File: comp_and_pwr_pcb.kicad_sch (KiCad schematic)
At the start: 127 parts, among them IC1 TPS5430MDDAREP, IC2 ICM-42688-P, IC3 LTC4415EDHC#TRPBF, IC4 TPS259531DSGR, IC5 BMP388, IC6 W25Q32JVSSIQ, IC7 TPS62743YFPR, J1 USB4216-03-A, J2 BATTERY_CONN, J3 SWD_CONN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

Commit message: Replaced files and updated project
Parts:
- removed BWSMA-KE-P1, BWSMA-KE-P2: ~, Connector_Coaxial:SMA_BAT_Wireless_BWSMA-KWE-Z001, symbol My:BWSMA-KE-P001
- removed F3: 05200101Z, 05200101Z:05200101Z, symbol 05200101Z:05200101Z
- added F1: Fuse_Small, Fuse:Fuse_0402_1005Metric, symbol Device:Fuse_Small
- added J10, J9: Conn_01x02, TerminalBlock_4Ucon:TerminalBlock_4Ucon_1x02_P3.50mm_Vertical, symbol Connector_Generic:Conn_01x02
- added J11, J12: Conn_Coaxial, Connector_Coaxial:SMA_Molex_73251-2200_Horizontal, symbol Connector:Conn_Coaxial
- added R24: 4.7kΩ, Resistor_SMD:R_0402_1005Metric, symbol Device:R
- E22-400M22S1: footprint E22-400M22S1:E22-400MM22S -> E22-400M22S:E22-400M22S
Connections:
- net +3.3V: now also R24.1
- net +BATT: now also F1.2
- net GND: now also J10.2 (Pin_2), J11.2 (Ext), J12.2 (Ext), J9.2 (Pin_2); no longer Q7.2 (S), Q9.2 (S)
- net I2C_SCL: now also R24.2
- net at J2.2 (Pin_2): now also F1.1
- net at D5.2 (A2), U2.11 (RF_IN): now also J12.1 (In)
- net at E22-400M22S1.21 (ANT): now also J11.1 (In)
- new net: J9.1 (Pin_1), Q9.2 (S)
- new net: J10.1 (Pin_1), Q7.2 (S)
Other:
- moved on the sheet: D5, Q7, Q8, R57, R58, R59, R60, TX2

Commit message: Initial KiCad project commit
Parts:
- removed C14: 10uF, Capacitor_SMD:C_1206_3216Metric, symbol Device:C
- removed IC7: TPS62743YFPR, TPS62743YFPR:BGA8C40P2X4_87X156X53, symbol TPS62743YFPR:TPS62743YFPR
- added C20: 0.1uF, Capacitor_SMD:C_0402_1005Metric, symbol Device:C
- added C23: 4.7uF, Capacitor_SMD:C_0603_1608Metric, symbol Device:C
- added C24: 10uF, Capacitor_SMD:C_1206_3216Metric, symbol Device:C
- added H1, H2, H3, H4: MountingHole, MountingHole:MountingHole_3.2mm_M3, symbol Mechanical:MountingHole
- added R25: 100k, Resistor_SMD:R_0402_1005Metric, symbol Device:R
- added R26: 6.8k, Resistor_SMD:R_0402_1005Metric, symbol Device:R
- added R27: 26.1k, Resistor_SMD:R_0402_1005Metric, symbol Device:R
- added R29: 10k, Resistor_SMD:R_0402_1005Metric, symbol Device:R
- added U3: MP2307DN-LF-Z, MP2307DN-LF-Z:SOIC127P600X170-9N, symbol MP2307DN-LF-Z:MP2307DN-LF-Z
- BZ1: footprint Buzzer_Beeper:Buzzer_12x9.5RM7.6 -> Buzzer_Beeper:Buzzer_CUI_CPT-9019S-SMT
- C11: value 0.1uF -> 10uF; footprint Capacitor_SMD:C_0402_1005Metric -> Capacitor_SMD:C_1206_3216Metric
- C12: value 4.7uF -> 0.1nF; footprint Capacitor_SMD:C_0603_1608Metric -> Capacitor_SMD:C_0402_1005Metric
- C13: value 4.7uF -> 10uF; footprint Capacitor_SMD:C_0603_1608Metric -> Capacitor_SMD:C_1206_3216Metric
- L2: value 2.2uH -> 10uH
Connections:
- net +3.3V: now also R27.1, R29.2, U3.5 (FB)
- net +5V: now also R25.2, U3.2 (IN); no longer C12.1, C13.1
- net GND: now also Q7.2 (S), Q9.2 (S), C20.2, R26.2, R29.1, U3.4 (GND); no longer C12.2
- net at J9.1 (Pin_1): now also Q10.3 (D), R64.1; no longer Q9.2 (S)
- net at L2.1: now also C12.2, U3.3 (SW)
- net at Q8.3 (D), R60.1: now also J10.1 (Pin_1)
- new net: C23.1, U3.6 (COMP)
- new net: R25.1, U3.7 (EN)
- new net: C20.1, U3.8 (SS)
- new net: C23.2, R26.1
- new net: C24.1, R27.2
- new net: C13.1, C24.2
- new net 3.3V_BS: C12.1, U3.1 (BS)
- no-connect marks 38 -> 39
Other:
- note added: "HOLES"
- moved on the sheet: C10, IC3, R10, R11, R21, R9

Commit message: pfc mistakes fixed
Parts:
- added C14: 10uF, Capacitor_SMD:C_0402_1005Metric, symbol Device:C_Small
- added C25: 100nF, Capacitor_SMD:C_0402_1005Metric, symbol Device:C_Small
- added R30: 10K, Resistor_SMD:R_0402_1005Metric, symbol Device:R
- R24: value 4.7kΩ -> 5k
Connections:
- net +3.3V: now also C24.1, R27.2, C14.2, C25.1, R30.1; no longer R24.1, R27.1, R29.2, U3.5 (FB)
- net +5V: now also IC3.20 (OUT2_3); no longer IC3.19 (IN2_3)
- net 5V_BATT: now also IC3.19 (IN2_3); no longer IC3.20 (OUT2_3)
- net GND: now also R24.2, R59.2, R61.2, C14.1, C25.2; no longer C7.2, IC4.7 (ILM)
- net I2C_SCL: no longer R24.2
- net PYRO1_SW: now also Q7.1 (G)
- net PYRO2_SW: now also Q9.1 (G)
- net USB_DM: no longer D1.1 (K)
- net USB_DP: no longer D2.2 (A)
- net WSP_SS: now also R30.2
- net at J1.A6 (DP1), J1.B6 (DP2), R5.2: now also D2.2 (A)
- net at C7.1, IC1.1 (BOOT): no longer IC1.8 (PH), L1.1
- net at J1.A7 (DN1), J1.B7 (DN2), R4.2: now also D1.1 (K)
- new net: R27.1, R29.2, U3.5 (FB)
- new net: IC4.7 (ILM), R24.1
- new net: C7.2, IC1.8 (PH), L1.1
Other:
- moved on the sheet: C7, D1, D2, R43, R44, R59, R61, R7

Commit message: Just a commit
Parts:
- IC3: footprint LTC4415EDHC#TRPBF:LTC4415IDHCTRPBF -> Package_DFN_QFN:DFN-18-1EP_3x5mm_P0.5mm_EP1.66x4.4mm
- Q1: footprint Package_TO_SOT_THT:TO-92_Inline -> Package_TO_SOT_SMD:SOT-23
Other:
- moved on the sheet: C28, J7, R27, R28, R29

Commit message: Final commit?
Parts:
- removed Q7, Q9: 2N7002Q-7-F, Package_TO_SOT_SMD:SOT-23, symbol 2N7002Q-7-F:2N7002Q-7-F
- removed R28: 100k, Resistor_SMD:R_0402_1005Metric, symbol Device:R
- added Q2, Q3: BSS138, Package_TO_SOT_SMD:SOT-23, symbol Transistor_FET:BSS138
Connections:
- net GND: now also Q2.2 (S), Q3.2 (S)
- net PYRO1_SW: now also Q3.1 (G)
- net PYRO2_SW: now also Q2.1 (G)
- net RXEN: no longer U1.30 (GPIO19)
- net TXEN: no longer U1.29 (GPIO18)
- net at R57.2, R58.2: now also Q3.3 (D)
- net at R62.2, R63.2: now also Q2.3 (D)
- no-connect marks 39 -> 41
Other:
- moved on the sheet: J10, J9, R59, R61

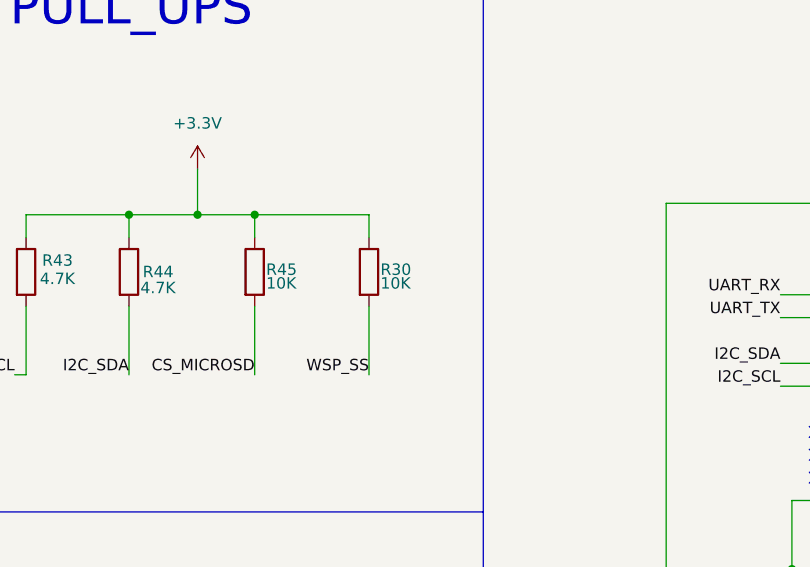
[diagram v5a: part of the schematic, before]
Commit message: R28 deleted
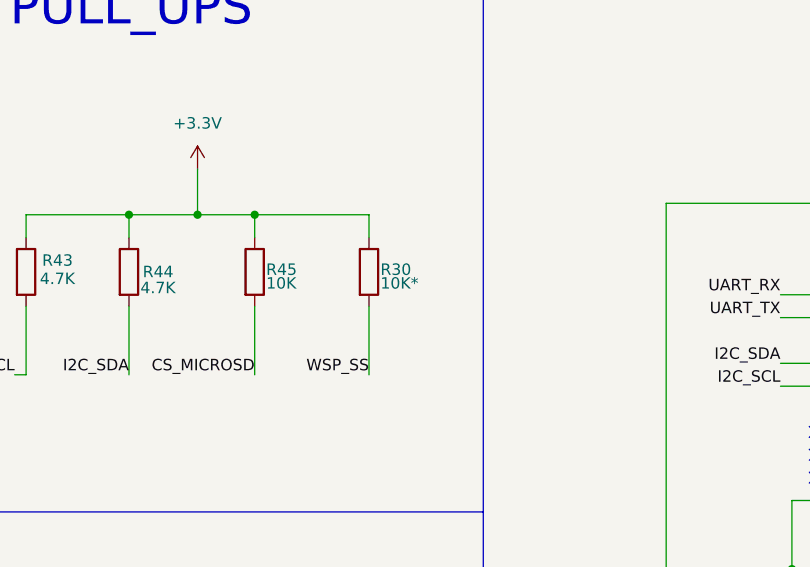
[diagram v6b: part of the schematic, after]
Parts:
- R30: value 10K -> 10K*
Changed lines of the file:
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@@
 			)
 		)
-		(property "Value" "10K"
+		(property "Value" "10K*"
 			(at 361.95 123.19 0)
 			(effects

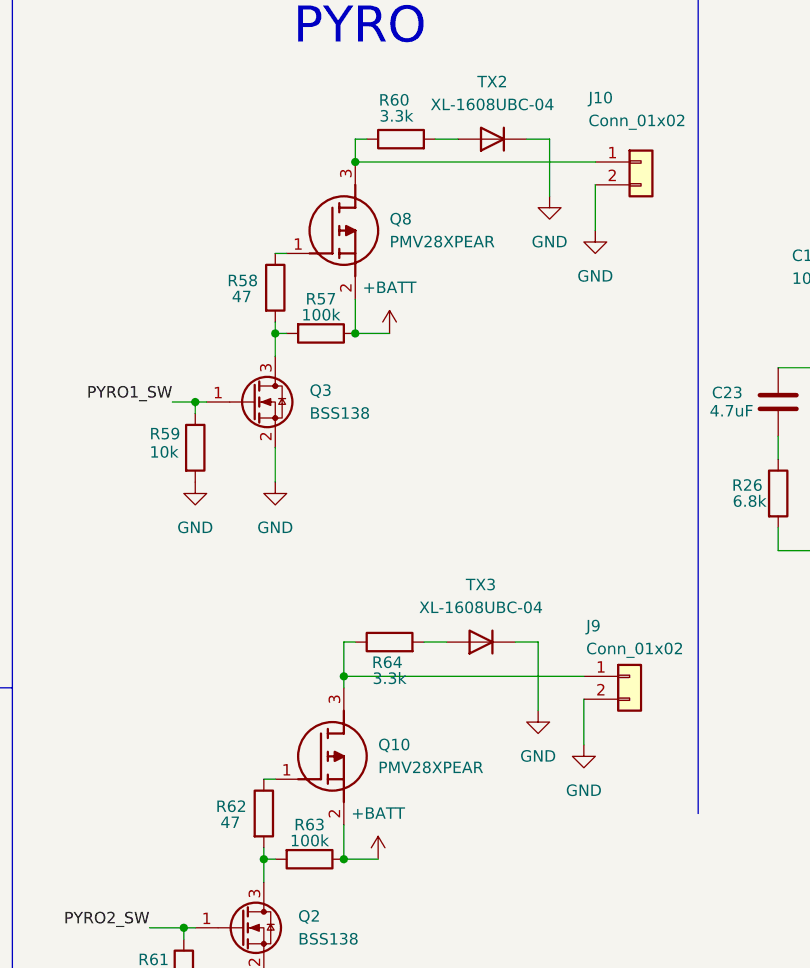
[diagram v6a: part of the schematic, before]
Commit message: Pyro mosfet change
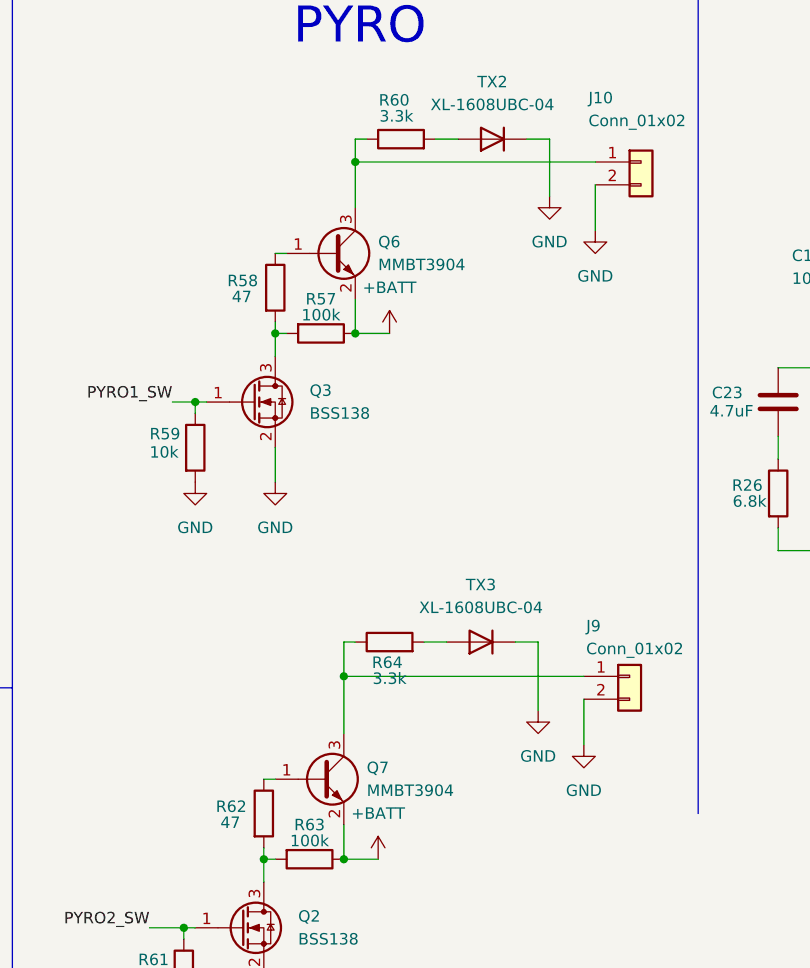
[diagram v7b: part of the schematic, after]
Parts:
- removed Q10, Q8: PMV28XPEAR, Package_TO_SOT_SMD:SOT-23, symbol PMV28XPEAR:PMV28XPEAR
- added Q6, Q7: MMBT3904, Package_TO_SOT_SMD:SOT-23, symbol Transistor_BJT:MMBT3904
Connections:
- net +BATT: now also Q6.2 (E), Q7.2 (E)
- net at J9.1 (Pin_1), R64.1: now also Q7.3 (C)
- net at R58.1: now also Q6.1 (B)
- net at R62.1: now also Q7.1 (B)
- net at J10.1 (Pin_1), R60.1: now also Q6.3 (C)

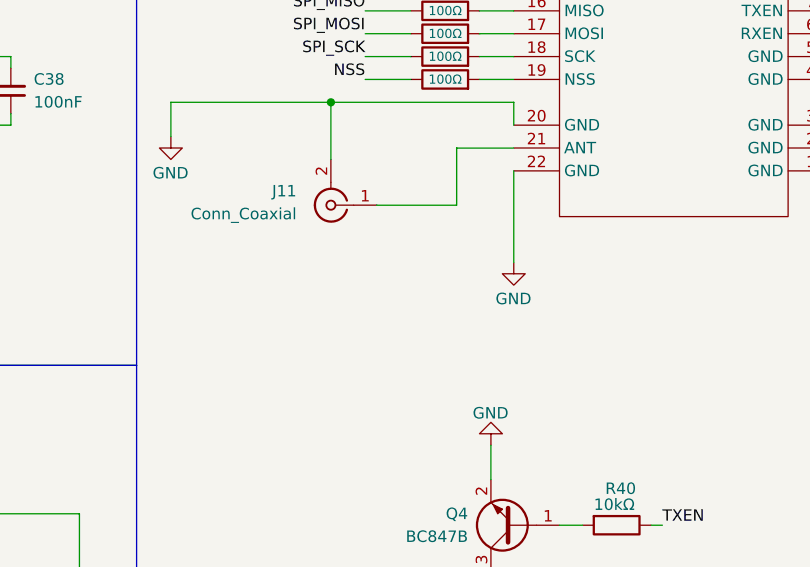
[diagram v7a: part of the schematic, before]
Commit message: TVS diodes fixed
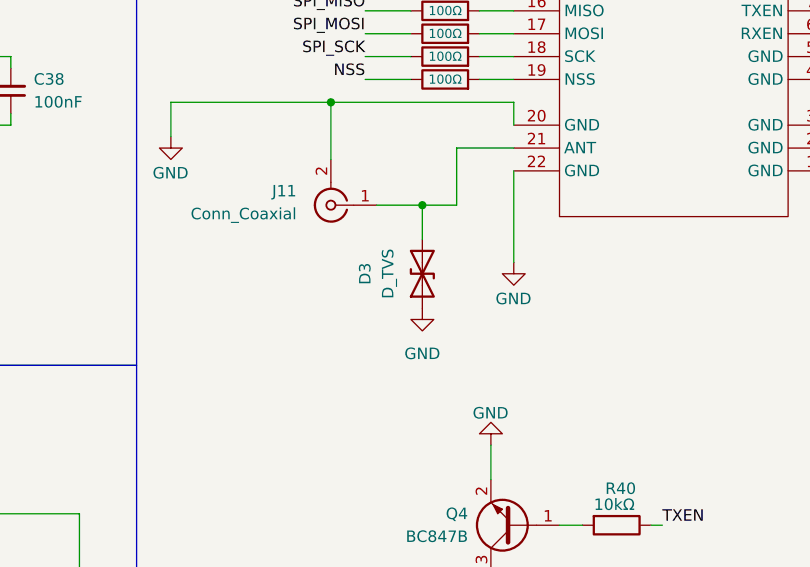
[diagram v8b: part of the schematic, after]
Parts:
- added D3: D_TVS, Diode_SMD:D_SOD-523, symbol Device:D_TVS
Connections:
- net GND: now also D3.1 (A1)
- net at E22-400M22S1.21 (ANT), J11.1 (In): now also D3.2 (A2)
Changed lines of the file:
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@@
 	)
 	(junction
+		(at 134.62 146.05)
+		(diameter 0)
+		(color 0 0 0 0)
+	)
+	(junction
 		(at 454.66 360.68)
 		(diameter 0)
@@
 	(wire
 		(pts
+			(xy 134.62 146.05) (xy 134.62 149.86)
+		)
+		(stroke
+			(width 0)
+			(type default)
+		)
+	)
+	(wire
+		(pts
 			(xy 516.89 311.15) (xy 511.81 311.15)
 		)
@@
 	(wire
 		(pts
+			(xy 134.62 146.05) (xy 138.43 146.05)
+		)
+		(stroke
+			(width 0)
+			(type default)
+		)
+	)
+	(wire
+		(pts
 			(xy 524.51 321.31) (xy 516.89 321.31)
 		)
@@
 	(wire
 		(pts
-			(xy 129.54 146.05) (xy 138.43 146.05)
+			(xy 129.54 146.05) (xy 134.62 146.05)
 		)
 		(stroke
@@
 	)
 	(symbol
+		(lib_id "power:GND")
+		(at 134.62 157.48 0)
+		(unit 1)
+		(exclude_from_sim no)
+		(in_bom yes)
+		(on_board yes)
+		(dnp no)
+		(fields_autoplaced yes)
+		(property "Reference" "#PWR098"
+			(at 134.62 163.83 0)
+			(effects
+				(font
+					(size 1.27 1.27)
+				)
+				(hide yes)
+			)
+		)
+		(property "Value" "GND"
+			(at 134.62 162.56 0)
+			(effects
+				(font
+					(size 1.27 1.27)
+				)
+			)
+		)
+		(property "Footprint" ""
+			(at 134.62 157.48 0)
+			(effects
+				(font
+					(size 1.27 1.27)
+				)
+				(hide yes)
+			)
+		)
+		(property "Datasheet" ""
+			(at 134.62 157.48 0)
+			(effects
+				(font
+					(size 1.27 1.27)
+				)
+				(hide yes)
+			)
+		)
+		(property "Description" "Power symbol creates a global label with name \"GND\" , ground"
+			(at 134.62 157.48 0)
+			(effects
+				(font
+					(size 1.27 1.27)
+				)
+				(hide yes)
+			)
+		)
+		(pin "1"
+		)
+		(instances
+			(project "comp_and_pwr_pcb"
+				(path "/ae870f52-69c5-42d4-a96b-91dd3b52c883"
+					(reference "#PWR098")
+					(unit 1)
+				)
+			)
+		)
+	)
+	(symbol
 		(lib_id "Device:R")
 		(at 241.3 381 90)
@@
 					(unit 1)
 				)
+			)
+		)
+	)
+	(symbol
+		(lib_id "Device:D_TVS")
+		(at 134.62 153.67 90)
+		(unit 1)
+		(exclude_from_sim no)
+		(in_bom yes)
+		(on_board yes)
+		(dnp no)
+		(fields_autoplaced yes)
+		(property "Reference" "D3"
+			(at 128.27 153.67 0)
+			(effects
+				(font
+					(size 1.27 1.27)
+				)
+			)
+		)
+		(property "Value" "D_TVS"
+			(at 130.81 153.67 0)
+			(effects
+				(font
+					(size 1.27 1.27)
+				)
+			)
+		)
+		(property "Footprint" "Diode_SMD:D_SOD-523"
+			(at 134.62 153.67 0)
+			(effects
+				(font
+					(size 1.27 1.27)
+				)
+				(hide yes)
+			)
+		)
+		(property "Datasheet" "~"
+			(at 134.62 153.67 0)
+			(effects
+				(font
+					(size 1.27 1.27)
+				)
+				(hide yes)
+			)
+		)
+		(property "Description" "Bidirectional transient-voltage-suppression diode"
+			(at 134.62 153.67 0)
+			(effects
+				(font
+					(size 1.27 1.27)
+				)
+				(hide yes)
+			)
+		)
+		(pin "2"
+		)
+		(pin "1"
+		)
+		(instances
+			(project "comp_and_pwr_pcb"
+				(path "/ae870f52-69c5-42d4-a96b-91dd3b52c883"
+					(reference "D3")
+					(unit 1)
+				)
